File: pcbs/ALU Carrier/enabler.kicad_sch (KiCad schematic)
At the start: 2 parts, among them U7001 74HC14, U7002 74HC08

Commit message: Working towards the connectors
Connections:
- net Cycle2: now also U7001.13; no longer U7001.1
- net Cycle3: now also U7001.11; no longer U7001.3
- net GND: now also U7001.1, U7001.3; no longer U7001.11, U7001.13
- net at U7001.4: no longer U7002.2
- net at U7002.1: now also U7001.12; no longer U7001.2
- net at U7001.10: now also U7002.2
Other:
- moved on the sheet: U7001A, U7001B, U7001E, U7001F
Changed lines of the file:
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@@
 	(symbol
 		(lib_id "74xx:74HC14")
-		(at 80.01 87.63 0)
+		(at 181.61 100.33 0)
 		(unit 2)
 		(exclude_from_sim no)
@@
 		(fields_autoplaced yes)
 		(property "Reference" "U7001"
-			(at 80.01 78.74 0)
+			(at 181.61 91.44 0)
 			(effects
 				(font
@@
 		)
 		(property "Value" "74HC14"
-			(at 80.01 81.28 0)
+			(at 181.61 93.98 0)
 			(effects
 				(font
@@
 		)
 		(property "Footprint" "Package_SO:SOIC-14_3.9x8.7mm_P1.27mm"
-			(at 80.01 87.63 0)
+			(at 181.61 100.33 0)
 			(effects
 				(font
@@
 		)
 		(property "Datasheet" "https://www.lcsc.com/datasheet/lcsc_datasheet_2407241044_Nexperia-74HC14D-653_C5605.pdf"
-			(at 80.01 87.63 0)
+			(at 181.61 100.33 0)
 			(effects
 				(font
@@
 		)
 		(property "Description" "Hex inverter schmitt trigger"
-			(at 80.01 87.63 0)
+			(at 181.61 100.33 0)
 			(effects
 				(font
@@
 		)
 		(property "LCSC" "C5605"
-			(at 80.01 87.63 0)
+			(at 181.61 100.33 0)
 			(effects
 				(font
@@
 	(symbol
 		(lib_id "74xx:74HC14")
-		(at 80.01 62.23 0)
+		(at 181.61 87.63 0)
 		(unit 1)
 		(exclude_from_sim no)
@@
 		(fields_autoplaced yes)
 		(property "Reference" "U7001"
-			(at 80.01 53.34 0)
+			(at 181.61 78.74 0)
 			(effects
 				(font
@@
 		)
 		(property "Value" "74HC14"
-			(at 80.01 55.88 0)
+			(at 181.61 81.28 0)
 			(effects
 				(font
@@
 		)
 		(property "Footprint" "Package_SO:SOIC-14_3.9x8.7mm_P1.27mm"
-			(at 80.01 62.23 0)
+			(at 181.61 87.63 0)
 			(effects
 				(font
@@
 		)
 		(property "Datasheet" "https://www.lcsc.com/datasheet/lcsc_datasheet_2407241044_Nexperia-74HC14D-653_C5605.pdf"
-			(at 80.01 62.23 0)
+			(at 181.61 87.63 0)
 			(effects
 				(font
@@
 		)
 		(property "Description" "Hex inverter schmitt trigger"
-			(at 80.01 62.23 0)
+			(at 181.61 87.63 0)
 			(effects
 				(font
@@
 		)
 		(property "LCSC" "C5605"
-			(at 80.01 62.23 0)
+			(at 181.61 87.63 0)
 			(effects
 				(font
@@
 	(symbol
 		(lib_id "74xx:74HC14")
-		(at 181.61 100.33 0)
+		(at 80.01 62.23 0)
 		(unit 6)
 		(exclude_from_sim no)
@@
 		(fields_autoplaced yes)
 		(property "Reference" "U7001"
-			(at 181.61 91.44 0)
+			(at 80.01 53.34 0)
 			(effects
 				(font
@@
 		)
 		(property "Value" "74HC14"
-			(at 181.61 93.98 0)
+			(at 80.01 55.88 0)
 			(effects
 				(font
@@
 		)
 		(property "Footprint" "Package_SO:SOIC-14_3.9x8.7mm_P1.27mm"
-			(at 181.61 100.33 0)
+			(at 80.01 62.23 0)
 			(effects
 				(font
@@
 		)
 		(property "Datasheet" "https://www.lcsc.com/datasheet/lcsc_datasheet_2407241044_Nexperia-74HC14D-653_C5605.pdf"
-			(at 181.61 100.33 0)
+			(at 80.01 62.23 0)
 			(effects
 				(font
@@
 		)
 		(property "Description" "Hex inverter schmitt trigger"
-			(at 181.61 100.33 0)
+			(at 80.01 62.23 0)
 			(effects
 				(font
@@
 		)
 		(property "LCSC" "C5605"
-			(at 181.61 100.33 0)
+			(at 80.01 62.23 0)
 			(effects
 				(font
@@
 	(symbol
 		(lib_id "74xx:74HC14")
-		(at 181.61 87.63 0)
+		(at 80.01 87.63 0)
 		(unit 5)
 		(exclude_from_sim no)
@@
 		(fields_autoplaced yes)
 		(property "Reference" "U7001"
-			(at 181.61 78.74 0)
+			(at 80.01 78.74 0)
 			(effects
 				(font
@@
 		)
 		(property "Value" "74HC14"
-			(at 181.61 81.28 0)
+			(at 80.01 81.28 0)
 			(effects
 				(font
@@
 		)
 		(property "Footprint" "Package_SO:SOIC-14_3.9x8.7mm_P1.27mm"
-			(at 181.61 87.63 0)
+			(at 80.01 87.63 0)
 			(effects
 				(font
@@
 		)
 		(property "Datasheet" "https://www.lcsc.com/datasheet/lcsc_datasheet_2407241044_Nexperia-74HC14D-653_C5605.pdf"
-			(at 181.61 87.63 0)
+			(at 80.01 87.63 0)
 			(effects
 				(font
@@
 		)
 		(property "Description" "Hex inverter schmitt trigger"
-			(at 181.61 87.63 0)
+			(at 80.01 87.63 0)
 			(effects
 				(font
@@
 		)
 		(property "LCSC" "C5605"
-			(at 181.61 87.63 0)
-			(effects
-				(font
+			(at 80.01 87.63 0)
+			(effects
+				(font

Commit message: Thinking some more
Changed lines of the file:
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@@
 		)
 	)
-	(hierarchical_label "Cycle[0..4]"
+	(hierarchical_label "Cycle[2..3]"
 		(shape input)
 		(at 46.99 49.53 180)

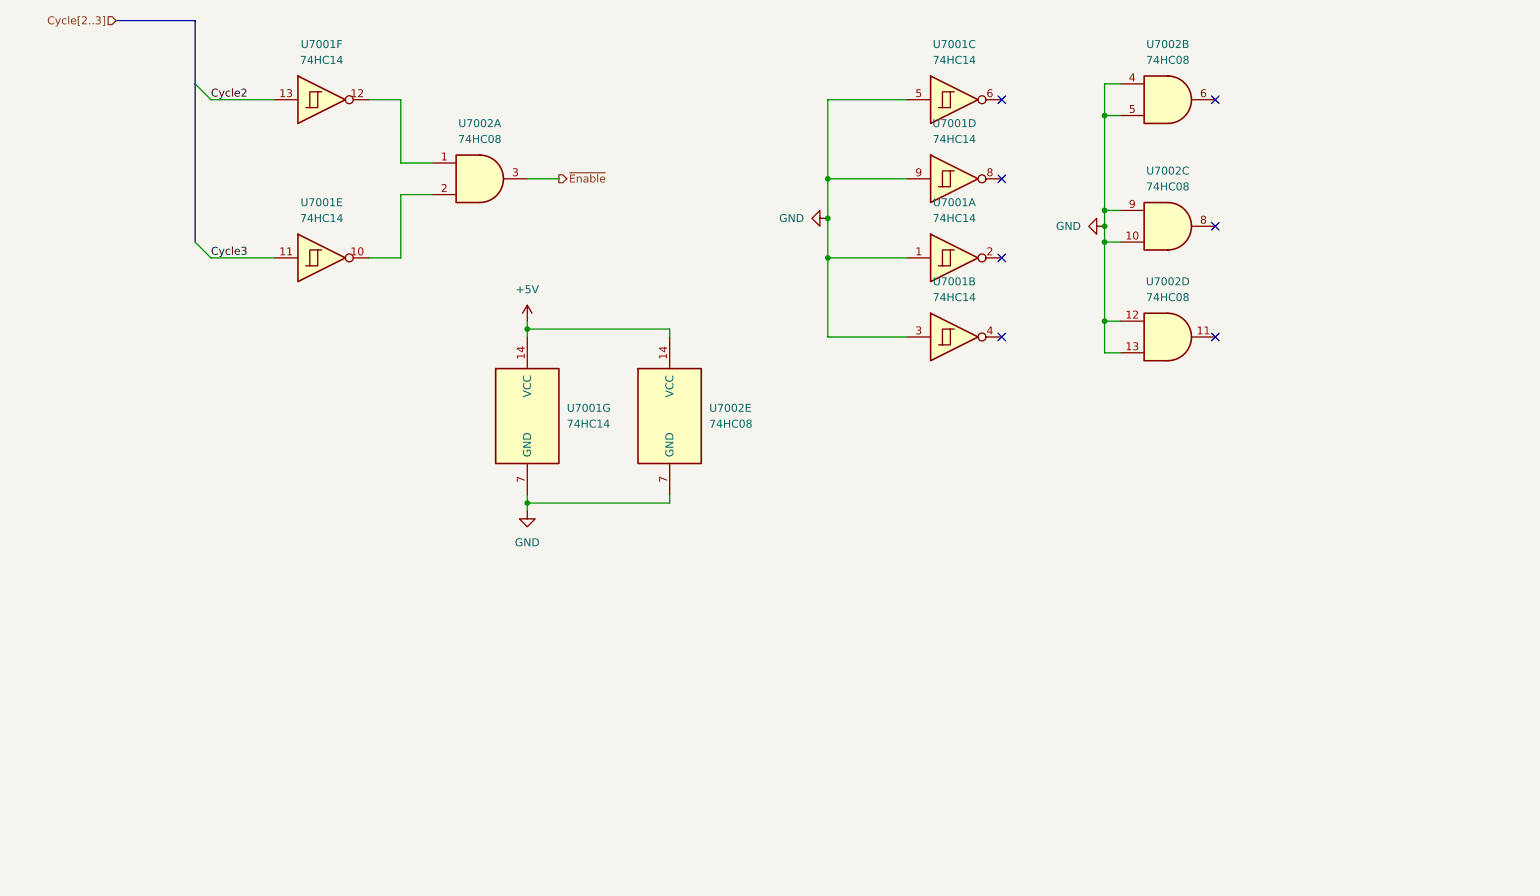
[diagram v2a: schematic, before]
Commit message: Spotted nasty error in enable logic
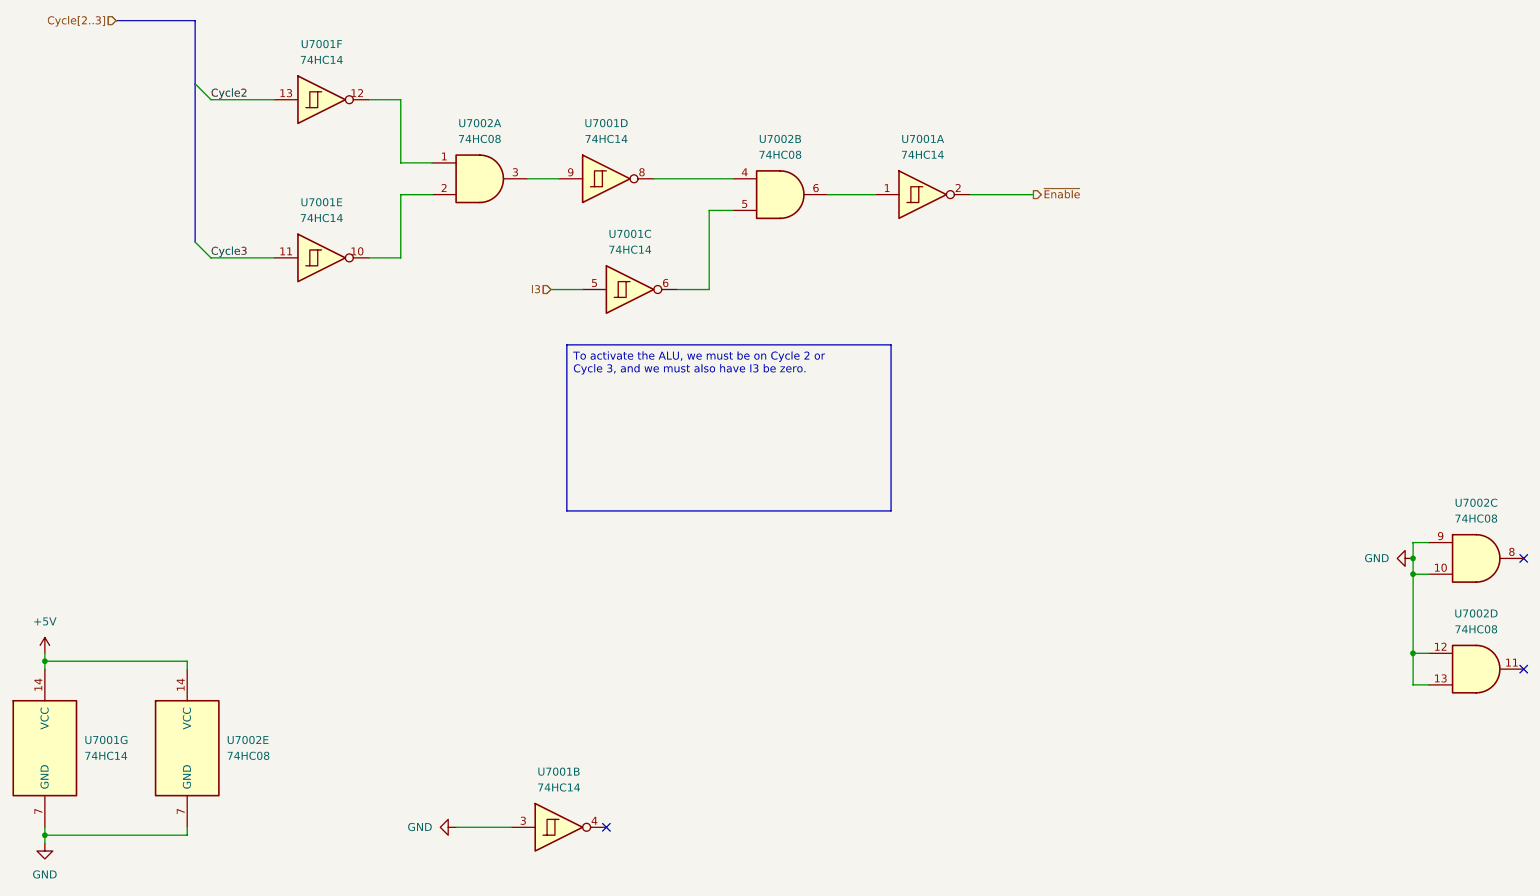
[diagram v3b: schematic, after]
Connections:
- net GND: no longer U7001.1, U7001.5, U7001.9, U7002.4, U7002.5
- net ~{Enable}: now also U7001.2; no longer U7002.3
- net at U7002.6: now also U7001.1
- net at U7001.6: now also U7002.5
- net at U7001.8: now also U7002.4
- new net: U7001.9, U7002.3
- new net I3: U7001.5
- no-connect marks 7 -> 3
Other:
- moved on the sheet: U7001A, U7001B, U7001C, U7001D, U7001G, U7002B, U7002C, U7002D, U7002E
